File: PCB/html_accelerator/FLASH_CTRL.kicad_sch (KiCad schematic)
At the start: 8 parts, among them U10 MX30LF1G28AD-TI, U2 AU6438BS, U3 MX30LF1G28AD-TI, U4 AU6438BS, U5 AU6438BS, U7 AU6438BS, U8 MX30LF1G28AD-TI, U9 MX30LF1G28AD-TI

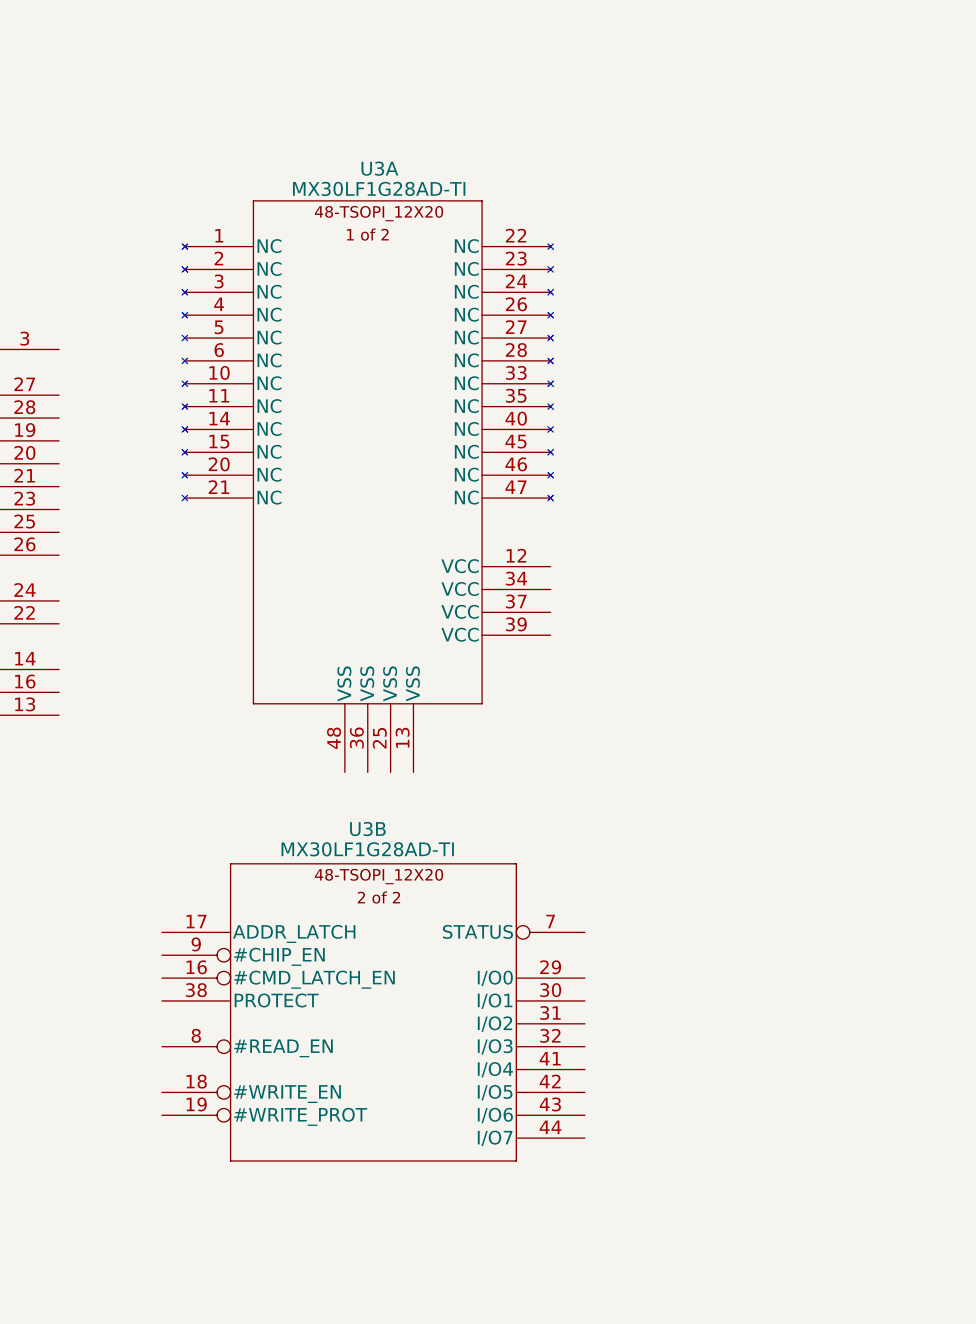
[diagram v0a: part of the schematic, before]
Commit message: block diagram, datasheet updates
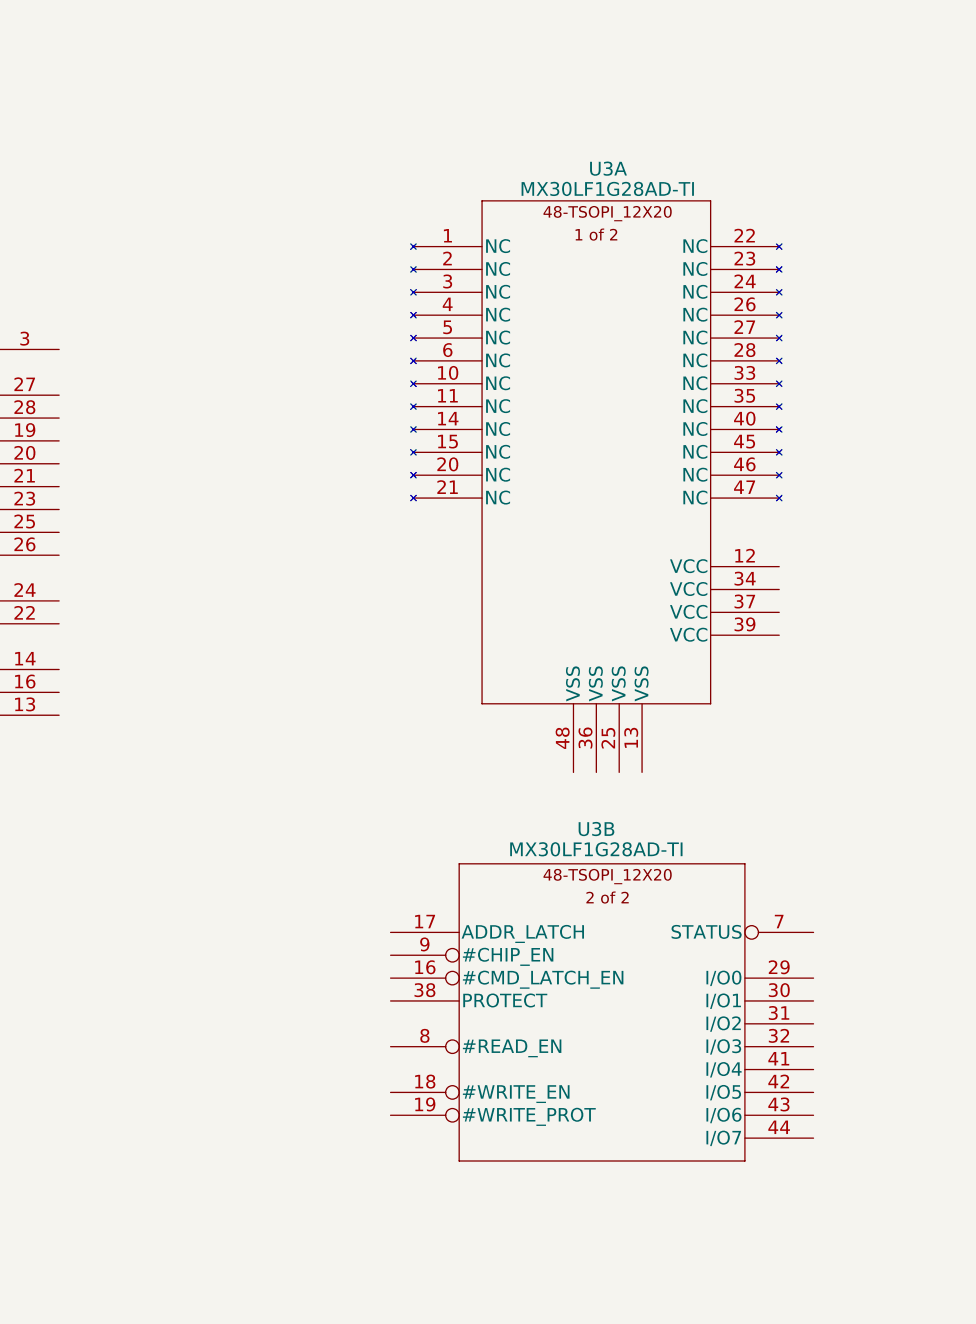
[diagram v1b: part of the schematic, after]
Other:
- moved on the sheet: U3A, U3B
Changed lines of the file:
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@@
     )
   )
-  (symbol (lib_id "html_accel_Symbols:MX30LF1G28AD-TI") (at 114.3 33.02 0) (unit 1)
+  (symbol (lib_id "html_accel_Symbols:MX30LF1G28AD-TI") (at 139.7 33.02 0) (unit 1)
     (in_bom yes) (on_board yes) (dnp no)
-    (property "Reference" "U3" (at 128.27 29.4958 0)
-      (effects (font (size 1.524 1.524)))
-    )
-    (property "Value" "MX30LF1G28AD-TI" (at 128.27 31.75 0)
-      (effects (font (size 1.524 1.524)))
-    )
-    (property "Footprint" "html_accel_footprints:MX30LF1G28AD-TI" (at 134.62 26.924 0)
-      (effects (font (size 1.524 1.524)) hide)
-    )
-    (property "Datasheet" "" (at 114.3 33.02 0)
+    (property "Reference" "U3" (at 153.67 29.4958 0)
+      (effects (font (size 1.524 1.524)))
+    )
+    (property "Value" "MX30LF1G28AD-TI" (at 153.67 31.75 0)
+      (effects (font (size 1.524 1.524)))
+    )
+    (property "Footprint" "html_accel_footprints:MX30LF1G28AD-TI" (at 160.02 26.924 0)
+      (effects (font (size 1.524 1.524)) hide)
+    )
+    (property "Datasheet" "" (at 139.7 33.02 0)
       (effects (font (size 1.524 1.524)))
     )
@@
     )
   )
-  (symbol (lib_id "html_accel_Symbols:MX30LF1G28AD-TI") (at 111.76 106.68 0) (unit 2)
+  (symbol (lib_id "html_accel_Symbols:MX30LF1G28AD-TI") (at 137.16 106.68 0) (unit 2)
     (in_bom yes) (on_board yes) (dnp no)
-    (property "Reference" "U3" (at 127 102.87 0)
-      (effects (font (size 1.524 1.524)))
-    )
-    (property "Value" "MX30LF1G28AD-TI" (at 127 105.1242 0)
-      (effects (font (size 1.524 1.524)))
-    )
-    (property "Footprint" "html_accel_footprints:MX30LF1G28AD-TI" (at 132.08 100.584 0)
-      (effects (font (size 1.524 1.524)) hide)
-    )
-    (property "Datasheet" "" (at 111.76 106.68 0)
-      (effects (font (size 1.524 1.524)))
-    )
+    (property "Reference" "U3" (at 152.4 102.87 0)
+      (effects (font (size 1.524 1.524)))
+    )
+    (property "Value" "MX30LF1G28AD-TI" (at 152.4 105.1242 0)
+      (effects (font (size 1.524 1.524)))
+    )
+    (property "Footprint" "html_accel_footprints:MX30LF1G28AD-TI" (at 157.48 100.584 0)
+      (effects (font (size 1.524 1.524)) hide)
+    )
+    (property "Datasheet" "" (at 137.16 106.68 0)
+      (effects (font (size 1.524 1.524)))
+    )
